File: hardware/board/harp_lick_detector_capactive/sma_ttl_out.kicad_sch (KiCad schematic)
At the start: 5 parts, among them J7 Conn_Coaxial, U10 CD74AC04

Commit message: update footprints; populate bom
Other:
- note added: "TODO: ESD protection."
- note added: "TTL Signal Buffering Reference."
- note removed: "Ref: https://www.sciencedirect.com/science/article/pii/S2405844021017771#fig10"
- company: (none) -> The Allen Institute for Neural Dynamics
- title: (none) -> Lickety Split Capacitive Lick Detector
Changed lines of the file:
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@@
 (kicad_sch (version 20230121) (generator eeschema)
   (paper "A4")
+  (title_block
+    (title "Lickety Split Capacitive Lick Detector")
+    (date "2023-09-01")
+    (rev "0.5")
+    (company "The Allen Institute for Neural Dynamics")
+  )
   (junction (at 131.445 92.075) (diameter 0) (color 0 0 0 0)
   )
@@
     (stroke (width 0) (type default))
   )
-  (text "Ref: https://www.sciencedirect.com/science/article/pii/S2405844021017771#fig10"
-    (at 177.165 163.195 0)
-    (effects (font (size 1.27 1.27)) (justify left bottom))
+  (text "TODO: ESD protection." (at 209.55 120.015 0)
+    (effects (font (size 2 2) (thickness 0.4) bold) (justify left bottom))
+  )
+  (text "TTL Signal Buffering Reference." (at 177.165 163.195 0)
+    (effects (font (size 1.27 1.27)) (justify left bottom) (href "https://www.sciencedirect.com/science/article/pii/S2405844021017771#fig10"))
   )
   (hierarchical_label "IN" (shape input) (at 109.855 92.075 180) (fields_autoplaced)

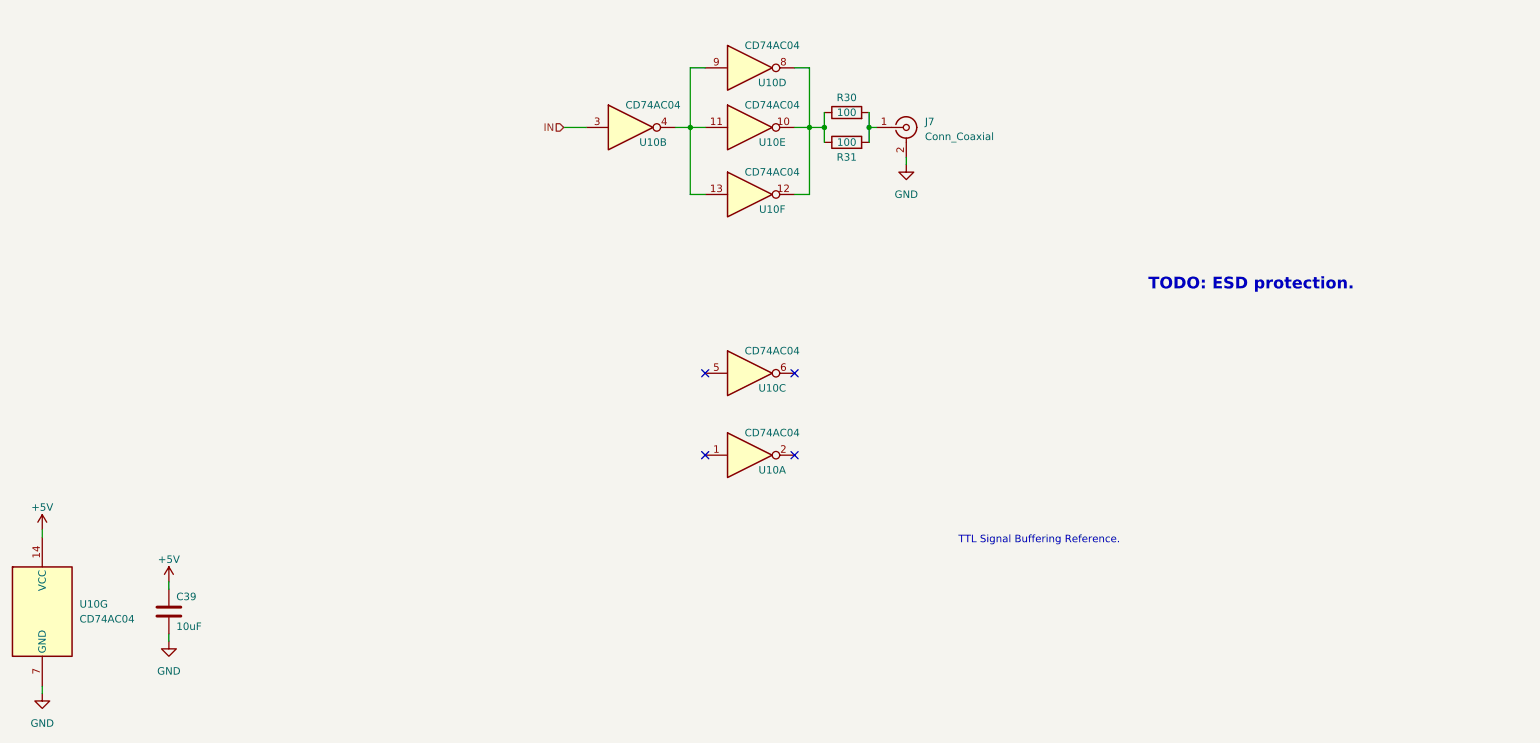
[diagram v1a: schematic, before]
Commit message: update ads7049 pinout
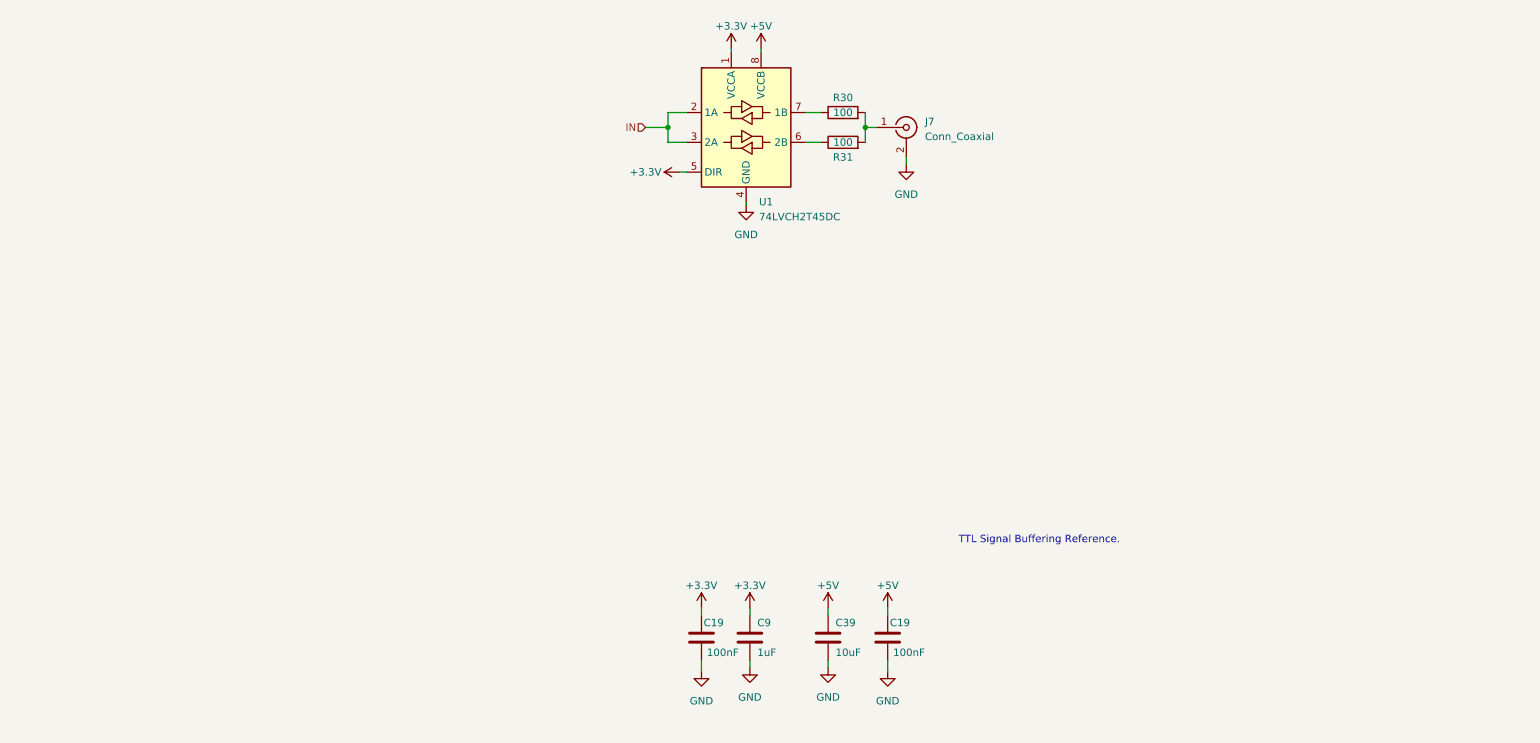
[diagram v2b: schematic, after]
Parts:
- removed U10: CD74AC04, Package_SO:SOIC-14_3.9x8.7mm_P1.27mm, symbol 74xx:74AHC04
- added C19 (x2): 100nF, Capacitor_SMD:C_0402_1005Metric, symbol Device:C
- added C9: 1uF, Capacitor_SMD:C_0402_1005Metric, symbol Device:C
- added U1: 74LVCH2T45DC, Package_SO:VSSOP-8_2.3x2mm_P0.5mm, symbol Logic_LevelTranslator:74LVCH2T45DC
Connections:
- net +5V: now also C19.2, U1.8 (VCCB)
- net GND: now also C19.1, C19.1, C9.2, U1.4 (GND)
- net IN: now also U1.2 (1A), U1.3 (2A)
- net at R31.1: now also U1.6 (2B); no longer R30.1
- new net: R30.1, U1.7 (1B)
- new net +3V3: C19.2, C9.1, U1.1 (VCCA), U1.5 (DIR)
- no-connect marks 4 -> 0
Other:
- note removed: "TODO: ESD protection."
- moved on the sheet: C39, R30, R31

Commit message: draft v0.6.0 board
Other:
- moved on the sheet: J7, R30, R31, U1

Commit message: make r0.6 board snapshot
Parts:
- C39: Alternate (none) -> CL21B106KOQNNNE
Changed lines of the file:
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@@
+      (effects (font (size 1.27 1.27)) hide)
+    )
+    (property "Alternate" "CL21B106KOQNNNE" (at 154.94 179.07 0)
       (effects (font (size 1.27 1.27)) hide)
     )

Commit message: draft v0.8 pcb layout
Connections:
- net +3V3 renamed +3.3V
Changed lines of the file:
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@@
       (effects (font (size 1.27 1.27)) hide)
     )
-    (property "Datasheet" "https://www.digikey.com/htmldatasheets/production/58667/0/0/1/consma002-smd-g.pdf" (at 168.275 91.44 0)
+    (property "Datasheet" " ~" (at 168.275 91.44 0)
       (effects (font (size 1.27 1.27)) hide)
     )

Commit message: update to new harp core
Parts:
- renumbered C9 to C53, C19 to C54, C19 to C55
